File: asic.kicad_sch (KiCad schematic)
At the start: 12 parts, among them U2 TXB0104RGYR, U5 MCP1824T-1802E, U6 MCP1824T-0802E

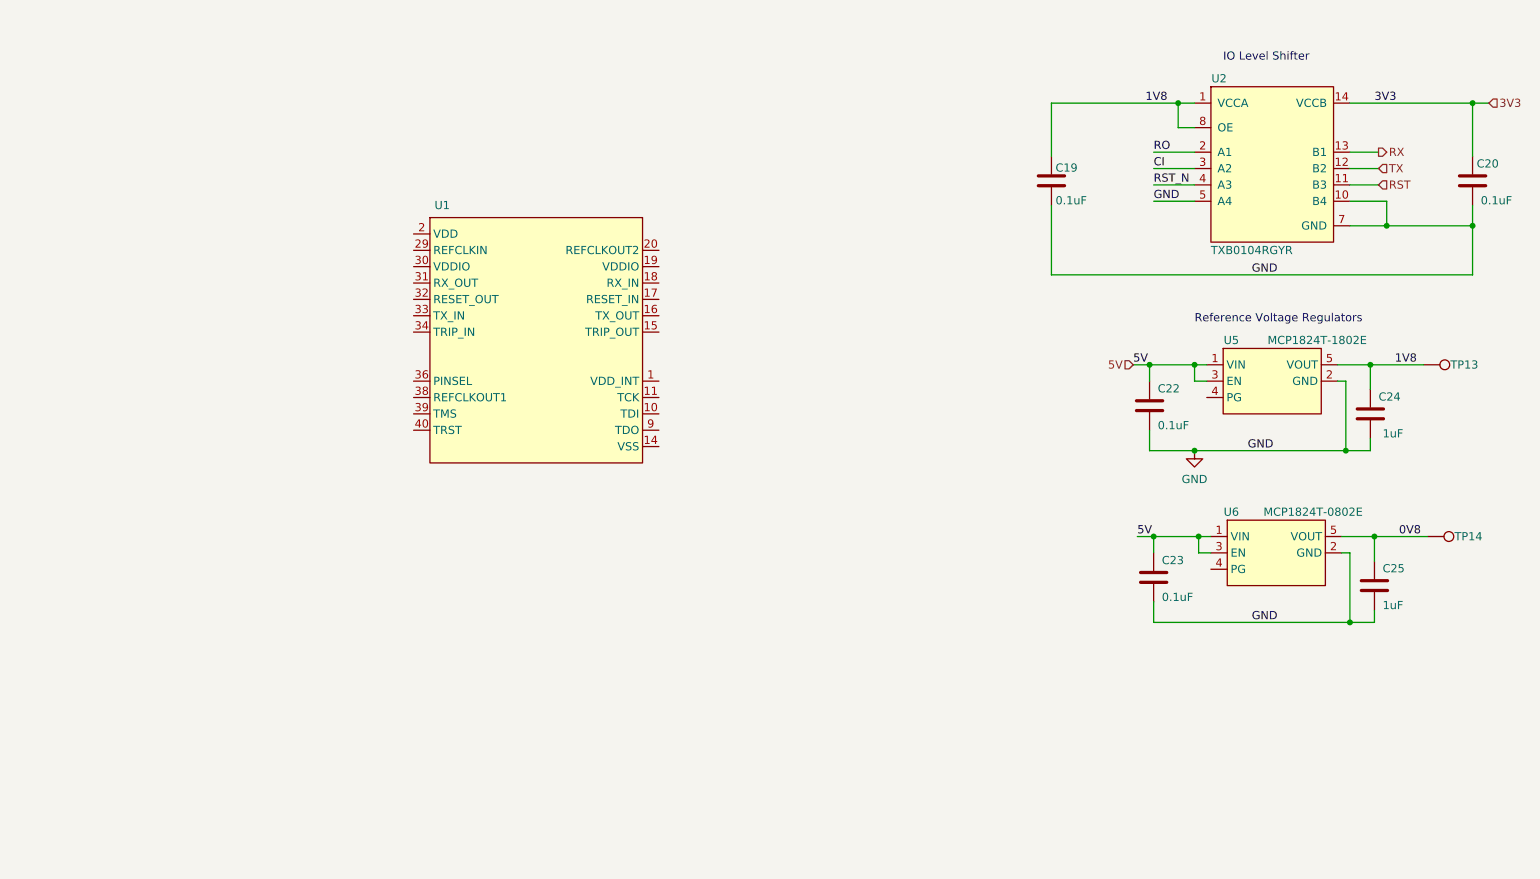
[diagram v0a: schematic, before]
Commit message: adding logo and docs
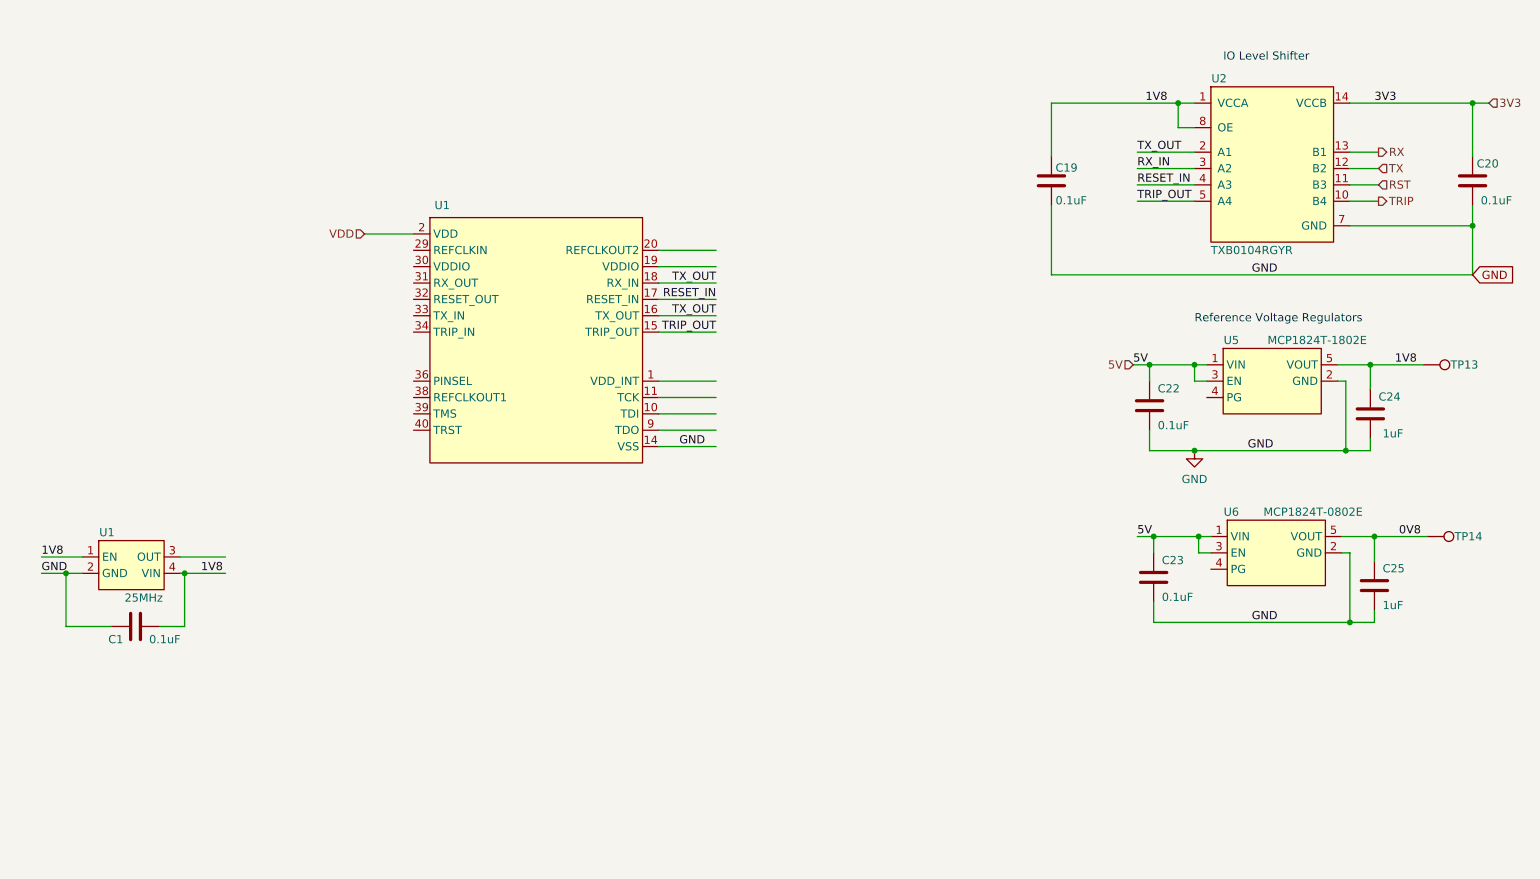
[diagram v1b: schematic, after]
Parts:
- added C1: 0.1uF, Capacitor_SMD:C_0402_1005Metric, symbol Device:C
- added U1: 25MHz, bitaxe:O 25,0-JO32-B-1V3-1-T1-LF, symbol bitaxe:oscillator
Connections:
- net RO is gone; now on net TX_OUT: U2.2 (A1)
- net RST_N is gone; now on net RESET_IN: U2.4 (A3)
- net 1V8: now also C1.2, U1.1 (EN), U1.4 (VIN)
- net GND: now also U1.14 (VSS), U1.21 (VSS), U1.22 (VSS), U1.23 (VSS), U1.24 (VSS), U1.25 (VSS), U1.26 (VSS), U1.27 (VSS), U1.28 (VSS), U1.35 (VSS), U1.41 (VSS), U1.42 (VSS), U1.43 (VSS), U1.44 (VSS), U1.45 (VSS), U1.46 (VSS), U1.47 (VSS), U1.48 (VSS), U1.49 (VSS), U1.50 (VSS), U1.51 (VSS), U1.52 (VSS), U1.53 (VSS), U1.54 (VSS), U1.55 (VSS), U1.56 (VSS), C1.1, U1.2 (GND); no longer U2.10 (B4), U2.5 (A4)
- net TRIP_OUT: now reaches U1.15 (TRIP_OUT)
- net TRIP_OUT: now also U2.5 (A4)
- net TX_OUT: now reaches U1.16 (TX_OUT)
- net TX_OUT: now also U1.18 (RX_IN)
- net RESET_IN: now reaches U1.17 (RESET_IN)
- net VDD: now reaches U1.2 (VDD), U1.3 (VDD), U1.4 (VDD), U1.5 (VDD), U1.6 (VDD), U1.7 (VDD), U1.8 (VDD)
- net CI renamed RX_IN
- new net TRIP: U2.10 (B4)

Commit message: added BZM2 footprint
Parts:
- U1: footprint (none) -> blockaxe:bzm2
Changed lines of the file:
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@@
       (effects (font (size 1.27 1.27)))
     )
-    (property "Footprint" "" (at 86.995 69.215 0)
+    (property "Footprint" "blockaxe:bzm2" (at 86.995 69.215 0)
       (effects (font (size 1.27 1.27)) hide)
     )

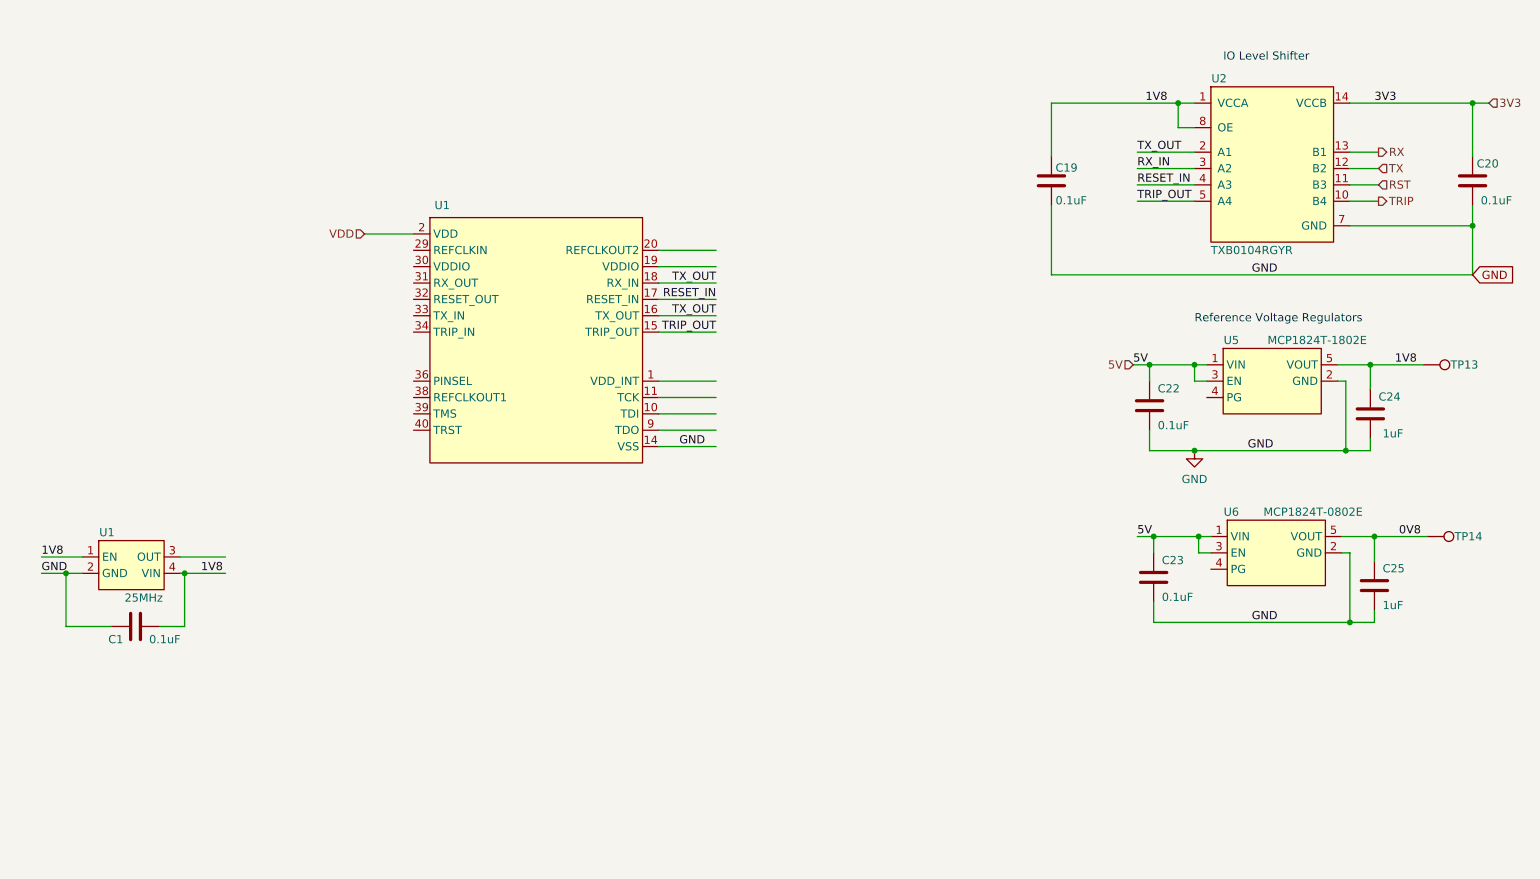
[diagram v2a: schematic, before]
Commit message: migrated over lots of bitaxe parts to blockaxe
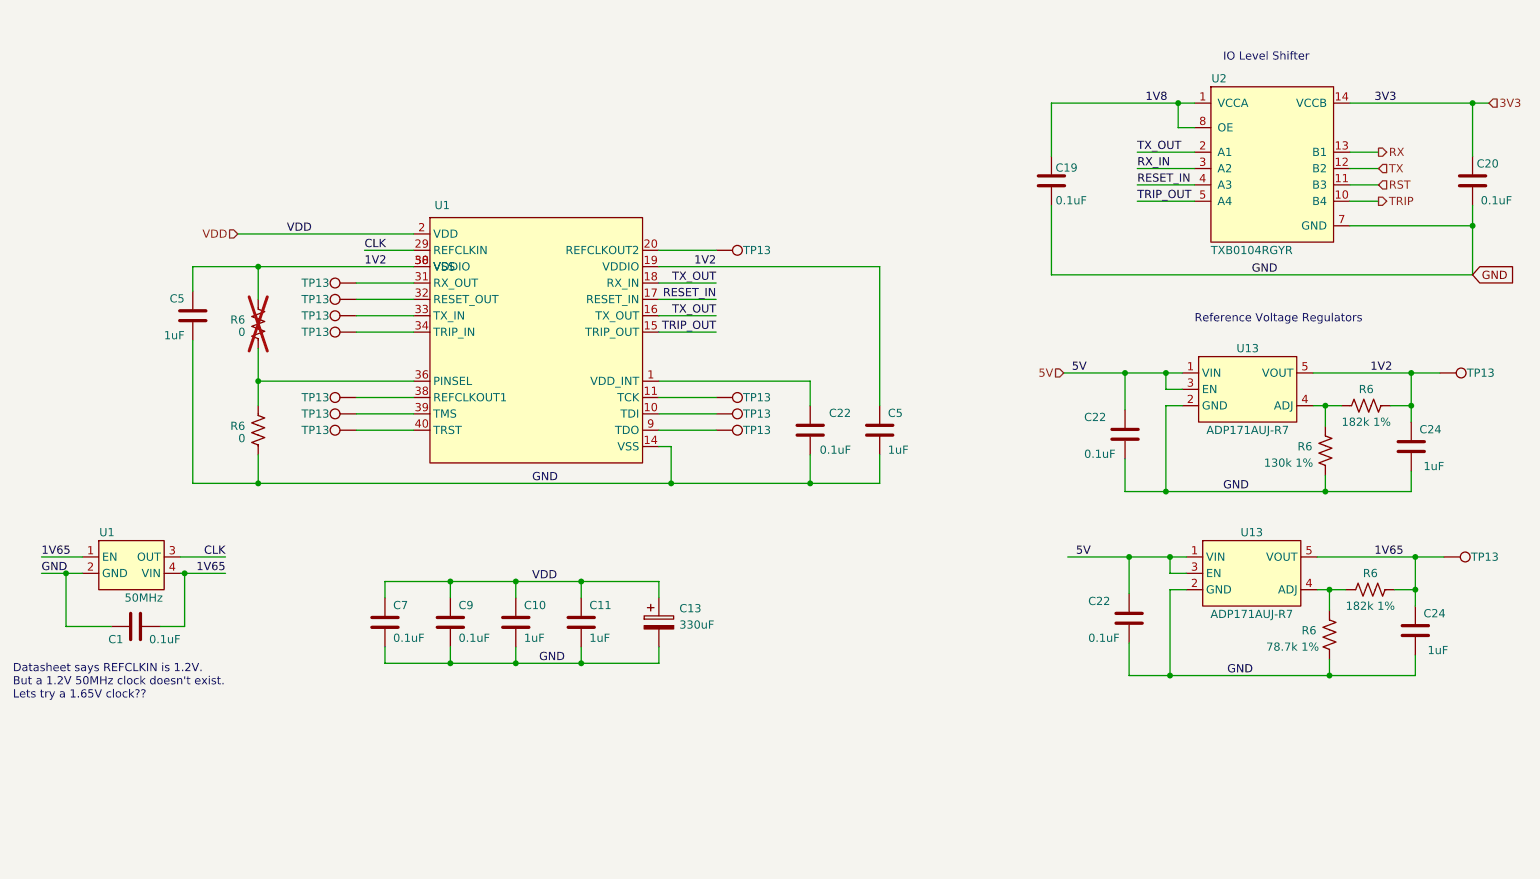
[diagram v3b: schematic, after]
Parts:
- removed C22, C23: 0.1uF, Capacitor_SMD:C_0402_1005Metric, symbol Device:C
- removed C24, C25: 1uF, Capacitor_SMD:C_0402_1005Metric, symbol Device:C
- removed TP13, TP14: TestPoint, TestPoint:TestPoint_Pad_D1.5mm, symbol Connector:TestPoint
- removed U5: MCP1824T-1802E, Package_TO_SOT_SMD:SOT-23-5, symbol bitaxe:MCP1824
- removed U6: MCP1824T-0802E, Package_TO_SOT_SMD:SOT-23-5, symbol bitaxe:MCP1824
- added C10, C11, C24 (x2), C5 (x2): 1uF, Capacitor_SMD:C_0402_1005Metric, symbol Device:C
- added C13: 330uF, Capacitor_Tantalum_SMD:CP_EIA-7343-31_Kemet-D_Pad2.25x2.55mm_HandSolder, symbol Device:C_Polarized
- added C22 (x3), C7, C9: 0.1uF, Capacitor_SMD:C_0402_1005Metric, symbol Device:C
- added R6 (x2): 182k 1%, Resistor_SMD:R_0402_1005Metric, symbol Device:R_US
- added R6: 78.7k 1%, Resistor_SMD:R_0402_1005Metric, symbol Device:R_US
- added R6 (x2): 0, Resistor_SMD:R_0402_1005Metric, symbol Device:R_US
- added R6: 130k 1%, Resistor_SMD:R_0402_1005Metric, symbol Device:R_US
- added TP13 (x13): TestPoint, TestPoint:TestPoint_Pad_D1.0mm, symbol Connector:TestPoint
- added U13 (x2): ADP171AUJ-R7, Package_TO_SOT_SMD:TSOT-23-5, symbol bitaxe:ADP171AUJ-R7
- U1: value 25MHz -> 50MHz; footprint bitaxe:O 25,0-JO32-B-1V3-1-T1-LF -> blockaxe:OSC_ECS-3225MV-500-CN-TR; DK 1908-O250-JO32-B-1V3-1-T1-LFCT-ND -> XC2889CT-ND; PARTNO O 25,0-JO32-B-1V3-1-T1-LF -> ECS-3225MV-500-CN-TR
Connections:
- net 1V8: no longer C1.2, U1.1 (EN), U1.4 (VIN)
- net 5V: now also C22.1, C22.1, U13.1 (VIN), U13.1 (VIN), U13.3 (EN), U13.3 (EN)
- net GND: now also U1.57 (VSS), C10.2, C11.2, C13.2, C22.2, C22.2, C22.2, C24.2, C24.2, C5.2, C5.2, C7.2, C9.2, R6.1, R6.1, R6.1, U13.2 (GND), U13.2 (GND); no longer U1.41 (VSS), U1.42 (VSS), U1.49 (VSS), U1.50 (VSS), U1.51 (VSS), U1.52 (VSS)
- net VDD: now also U1.41 (VDD), U1.42 (VDD), U1.49 (VDD), U1.50 (VDD), U1.51 (VDD), U1.52 (VDD), U1.59 (VDD), U1.60 (VDD), C10.1, C11.1, C13.1, C7.1, C9.1
- net at U1.1 (VDD_INT), U1.12 (VDD_INT): now also C22.1
- net at U1.10 (TDI): now also TP13.1
- net at U1.11 (TCK): now also TP13.1
- net 1V2: now reaches U1.19 (VDDIO)
- net 1V2: now also U1.30 (VDDIO), U1.58 (VSS), C24.1, C5.1, C5.1, R6.1, R6.2, TP13.1, U13.5 (VOUT)
- net at U1.20 (REFCLKOUT2): now also TP13.1
- net CLK: now reaches U1.29 (REFCLKIN)
- net CLK: now also U1.3 (OUT)
- net at U1.31 (RX_OUT): now also TP13.1
- net at U1.32 (RESET_OUT): now also TP13.1
- net at U1.33 (TX_IN): now also TP13.1
- net at U1.34 (TRIP_IN): now also TP13.1
- net at U1.36 (PINSEL): now also R6.1, R6.2
- net at U1.38 (REFCLKOUT1): now also TP13.1
- net at U1.39 (TMS): now also TP13.1
- net at U1.40 (TRST): now also TP13.1
- net at U1.9 (TDO): now also TP13.1
- new net: R6.2, R6.2, U13.4 (ADJ) (x2)
- new net 1V65: C1.2, C24.1, R6.1, TP13.1, U1.1 (EN), U1.4 (VIN), U13.5 (VOUT)
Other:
- note added: "Datasheet says REFCLKIN is 1.2V. But a 1.2V 50MHz clock doesn't exist. Lets try a 1.65V clock??"

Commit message: all the footprints are in?
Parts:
- U2: footprint bitaxe:TXB0104 -> blockaxe:TXB0104
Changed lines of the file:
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@@
       (effects (font (size 1.27 1.27)))
     )
-    (property "Footprint" "bitaxe:TXB0104" (at 246.38 90.805 0)
+    (property "Footprint" "blockaxe:TXB0104" (at 246.38 90.805 0)
       (effects (font (size 1.27 1.27)) (justify bottom) hide)
     )

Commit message: more placing and routing
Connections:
- net 5V is gone; now on net 3V3: C22.1, C22.1, U13.1 (VIN), U13.1 (VIN), U13.3 (EN), U13.3 (EN)
- net 1V2: no longer U1.58 (VSS)
- net GND: now also U1.58 (VSS)
- net at C22.1, U1.1 (VDD_INT_1): no longer U1.12 (VDD_INT)
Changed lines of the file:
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@@
     (effects (font (size 1.27 1.27)) (justify left bottom))
   )
-  (label "5V" (at 189.23 88.265 0) (fields_autoplaced)
+  (label "3V3" (at 188.595 116.84 0) (fields_autoplaced)
     (effects (font (size 1.27 1.27)) (justify left bottom))
   )
@@
     (effects (font (size 1.27 1.27)) (justify right bottom))
   )
+  (label "3V3" (at 187.96 88.265 0) (fields_autoplaced)
+    (effects (font (size 1.27 1.27)) (justify left bottom))
+  )
   (label "1V2" (at 79.375 71.755 0) (fields_autoplaced)
     (effects (font (size 1.27 1.27)) (justify left bottom))
@@
   )
   (label "GND" (at 212.725 106.68 0) (fields_autoplaced)
-    (effects (font (size 1.27 1.27)) (justify left bottom))
-  )
-  (label "5V" (at 189.865 116.84 0) (fields_autoplaced)
     (effects (font (size 1.27 1.27)) (justify left bottom))
   )
@@
   (hierarchical_label "TX" (shape input) (at 236.855 56.515 0) (fields_autoplaced)
     (effects (font (size 1.27 1.27)) (justify left))
-  )
-  (hierarchical_label "5V" (shape input) (at 187.96 88.265 180) (fields_autoplaced)
-    (effects (font (size 1.27 1.27)) (justify right))
   )
   (hierarchical_label "RX" (shape output) (at 236.855 53.975 0) (fields_autoplaced)
@@
       (effects (font (size 1.27 1.27)) hide)
     )
-    (pin "1")
     (pin "10")
     (pin "11")
@@
     (pin "40")
     (pin "9")
+    (pin "1")
     (pin "12")
     (pin "13")

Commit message: finished routing. switched back to THT barrel
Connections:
- net 1V8 is gone; now on net 1V2: C19.1, U2.1 (VCCA), U2.8 (OE)
- net RX_IN: now also U1.18 (RX_IN)
- net TX_OUT: no longer U1.18 (RX_IN)
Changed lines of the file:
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@@
     (effects (font (size 1.27 1.27)) (justify left bottom))
-  )
-  (label "TX_OUT" (at 133.985 74.295 180) (fields_autoplaced)
-    (effects (font (size 1.27 1.27)) (justify right bottom))
   )
   (label "3V3" (at 187.96 88.265 0) (fields_autoplaced)
@@
     (effects (font (size 1.27 1.27)) (justify left bottom))
   )
+  (label "RX_IN" (at 133.985 74.295 180) (fields_autoplaced)
+    (effects (font (size 1.27 1.27)) (justify right bottom))
+  )
   (label "TX_OUT" (at 133.985 79.375 180) (fields_autoplaced)
     (effects (font (size 1.27 1.27)) (justify right bottom))
@@
     (effects (font (size 1.27 1.27)) (justify left bottom))
   )
-  (label "1V8" (at 200.66 46.355 0) (fields_autoplaced)
+  (label "1V2" (at 200.66 46.355 0) (fields_autoplaced)
     (effects (font (size 1.27 1.27)) (justify left bottom))
   )
@@
       (project "blockaxe1"
         (path "/a166cb37-4e3a-4be5-b2da-277a3281a4de/9f287754-26df-4418-a7f4-7b5e0717668c"
-          (reference "U14") (unit 1)
-        )
-      )
+          (reference "Y1") (unit 1)
+        )
+      )

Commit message: added gerbers and BOM
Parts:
- R6: DK (none) -> 311-78.7KLRCT-ND; PARTNO (none) -> RC0402FR-0778K7L
- R6: DK (none) -> RMCF0402ZT0R00CT-ND; PARTNO (none) -> RMCF0402ZT0R00
- R6: DK (none) -> YAG2969CT-ND; PARTNO (none) -> RC0402FR-07130KL
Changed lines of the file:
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@@
       (effects (font (size 1.27 1.27)) hide)
     )
-    (property "DK" "" (at 229.235 128.905 0)
-      (effects (font (size 1.27 1.27)) hide)
-    )
-    (property "PARTNO" "" (at 229.235 128.905 0)
+    (property "DK" "311-78.7KLRCT-ND" (at 229.235 128.905 0)
+      (effects (font (size 1.27 1.27)) hide)
+    )
+    (property "PARTNO" "RC0402FR-0778K7L" (at 229.235 128.905 0)
       (effects (font (size 1.27 1.27)) hide)
     )
@@
       (effects (font (size 1.27 1.27)) hide)
     )
-    (property "DK" "" (at 62.865 97.155 0)
-      (effects (font (size 1.27 1.27)) hide)
-    )
-    (property "PARTNO" "" (at 62.865 97.155 0)
+    (property "DK" "RMCF0402ZT0R00CT-ND" (at 62.865 97.155 0)
+      (effects (font (size 1.27 1.27)) hide)
+    )
+    (property "PARTNO" "RMCF0402ZT0R00" (at 62.865 97.155 0)
       (effects (font (size 1.27 1.27)) hide)
     )
@@
       (effects (font (size 1.27 1.27)) hide)
     )
-    (property "DK" "" (at 228.6 100.33 0)
-      (effects (font (size 1.27 1.27)) hide)
-    )
-    (property "PARTNO" "" (at 228.6 100.33 0)
+    (property "DK" "YAG2969CT-ND" (at 228.6 100.33 0)
+      (effects (font (size 1.27 1.27)) hide)
+    )
+    (property "PARTNO" "RC0402FR-07130KL" (at 228.6 100.33 0)
       (effects (font (size 1.27 1.27)) hide)
     )
@@
       (effects (font (size 1.27 1.27)) hide)
     )
-    (property "DK" "" (at 62.865 80.645 0)
-      (effects (font (size 1.27 1.27)) hide)
-    )
-    (property "PARTNO" "" (at 62.865 80.645 0)
-      (effects (font (size 1.27 1.27)) hide)
-    )
+    (property "DK" "RMCF0402ZT0R00CT-ND" (at 62.865 80.645 0)
+      (effects (font (size 1.27 1.27)) hide)
+    )
+    (property "PARTNO" "RMCF0402ZT0R00" (at 62.865 80.645 0)
+      (effects (font (size 1.27 1.27)) hide)
+    )
